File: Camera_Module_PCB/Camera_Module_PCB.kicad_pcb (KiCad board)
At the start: 4 copper layers, 118 parts, among them J1 SS-52400-002, J2 Conn_01x02, J3 FFC2A32-24-T, SW1 SW_DIP_x01, SW2 SW_Push, SW3 SW_Push, U2 ESP32-S3R8, U4 MAX98357AETE_T, U5 AP3032KTR-G1, Y1 Q40,0-JXS10-8-10/10-FU-LF1

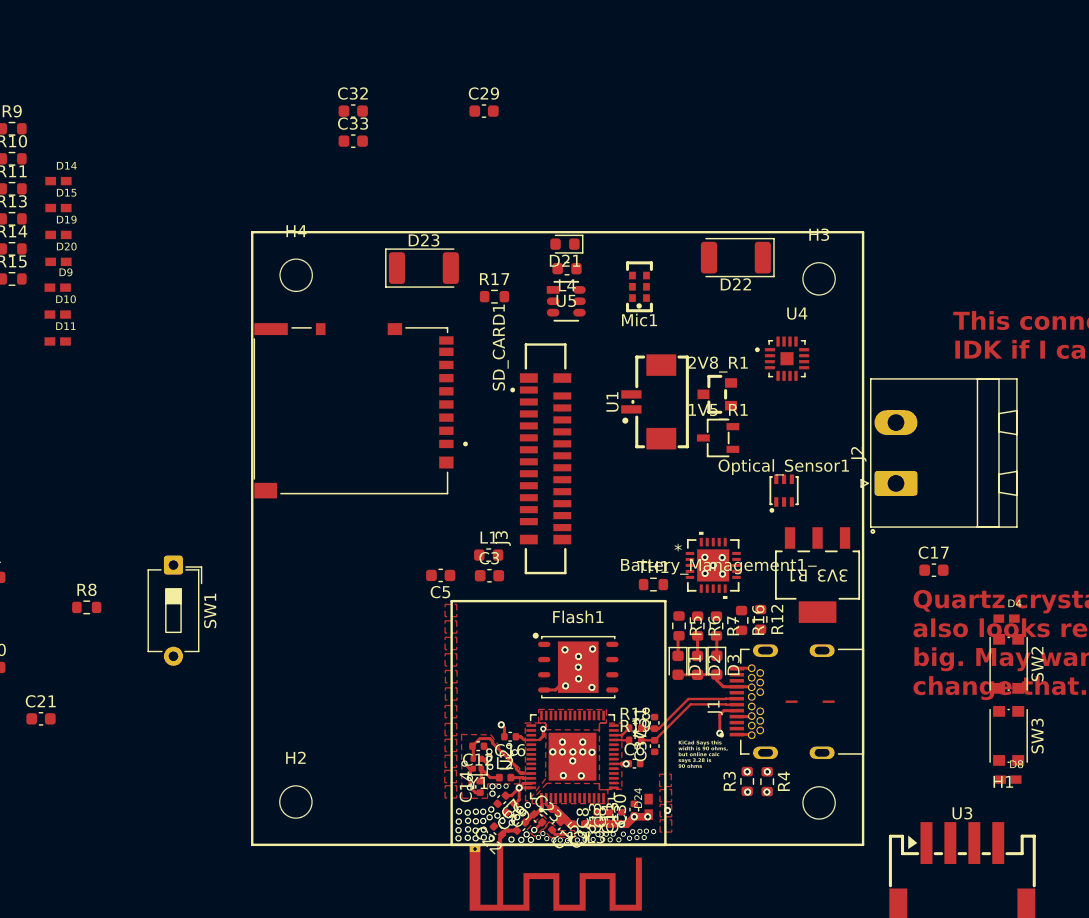
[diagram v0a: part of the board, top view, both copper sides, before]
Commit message: Finished Power Supply
The power supply was finished for the ESP32 Chip and the board as a whole. A large plain was constructed in the third layer of the PCB to hold the 3.3V power supply from the regulator. Multiple traces have begun to be routed out of the ESP32 chip to be connected later on.
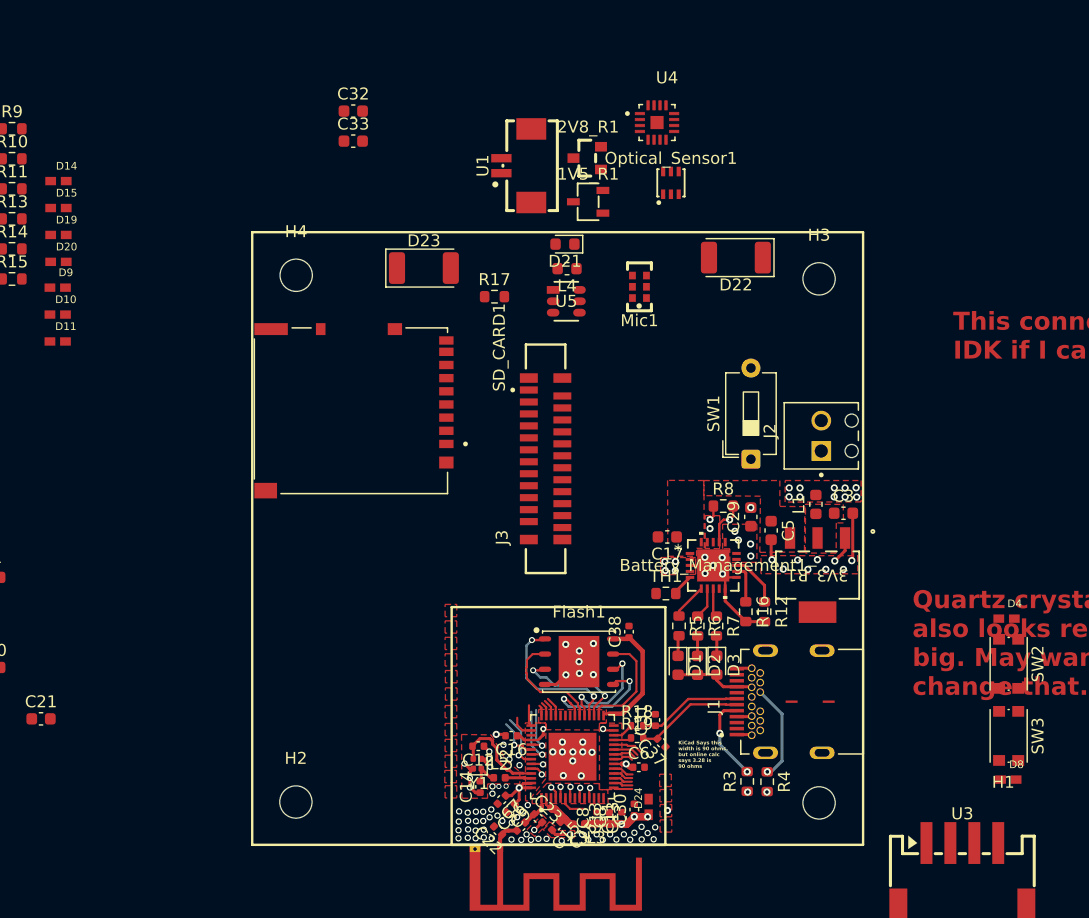
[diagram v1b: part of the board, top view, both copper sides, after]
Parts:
- added C38: 10uF, Capacitor_SMD:C_0402_1005Metric, F.Cu at (133.1, 84.2)
- J2: footprint Connector_Phoenix_MSTB:PhoenixContact_MSTBA_2,5_2-G-5,08_1x02_P5.08mm_Horizontal -> ESP32CAM_Foorprints:PHOENIX_1725656
- moved R8 53.9 mm to (141.0, 73.7)
- moved SW1 49.1 mm to (143.3, 69.8), turned to 90 degrees
- moved C29 40.6 mm to (143.3, 74.6), turned to 90 degrees
- moved C3 30.0 mm to (151.0, 74.3)
- moved C5 27.9 mm to (145.0, 75.7), turned to -90 degrees
- moved L1 27.7 mm to (148.7, 73.6), turned to 90 degrees
- moved Optical_Sensor1 27.4 mm to (136.6, 46.7)
- moved U4 22.5 mm to (135.4, 41.6)
- moved 2V8_R1 22.5 mm to (129.6, 44.6)
- moved U1 22.5 mm to (123.7, 45.2)
- moved 1V5_R1 22.5 mm to (129.7, 48.3)
- moved C17 22.5 mm to (136.3, 76.3), turned to 180 degrees
- moved J2 3.37 mm to (152.3, 70.6)
- moved TH1 1.28 mm to (136.2, 81.0)
- moved R16 0.81 mm to (142.8, 82.5)
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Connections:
- U2 pad 13: /SDA -> unconnected-(U2-GPIO8-Pad13)
- U2 pad 14: /SCL -> unconnected-(U2-GPIO9-Pad14)
- U2 pad 36: /Light_INT -> unconnected-(U2-SPICLK_N-Pad36)
- U2 pad 37: /LED_CT -> unconnected-(U2-SPICLK_P-Pad37)
- U2 pad 39: unconnected-(U2-GPIO34-Pad39) -> /Light_INT
- U2 pad 40: unconnected-(U2-GPIO35-Pad40) -> /LED_CT
- U2 pad 41: unconnected-(U2-GPIO36-Pad41) -> /SDA
- U2 pad 42: unconnected-(U2-GPIO37-Pad42) -> /SCL
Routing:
- net GND: track 16.4 -> 34.3 mm, vias 93 -> 96
- net Net-(Flash1-CS): track 0.00 -> 12.6 mm, vias 0 -> 2
- net /VDD_SPI: track 0.00 -> 10.6 mm
- net Net-(Flash1-DI(IO0)): track 0.00 -> 10.5 mm, vias 0 -> 2
- net /SPIWP: track 0.00 -> 9.92 mm, vias 0 -> 2
- net /Power Supply/CHG_EN: track 0.00 -> 9.61 mm, vias 0 -> 1
- net Net-(Flash1-DO(IO1)): track 0.00 -> 9.52 mm
- net /SPIHD: track 0.00 -> 9.05 mm
- net /SPICLK: track 0.00 -> 8.90 mm, vias 0 -> 2
- net /Power Supply/5V_USB: track 8.16 -> 15.7 mm, vias 0 -> 6
- net /LRCLK: track 0.00 -> 7.11 mm, vias 0 -> 1
- net /BCLK: track 0.00 -> 6.51 mm, vias 0 -> 1
- net Net-(U2-U0TXD): track 0.00 -> 4.96 mm, vias 0 -> 1
- net Net-(U2-U0RXD): track 0.00 -> 4.66 mm, vias 0 -> 1
- net Net-(Battery_Management1-PROG1): track 0.00 -> 4.42 mm
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- added copper zone on F.Cu, net /Power Supply/5V_USB
- added copper zone on In2.Cu, net /Power Supply/5V_USB
- added copper zone on F.Cu, net /Power Supply/VBAT
- added copper zone on In2.Cu, net /Power Supply/VBAT
- added copper zone on F.Cu, net Net-(3V3_R1-OUTPUT)
- added copper zone on F.Cu, net V_OUT_BM

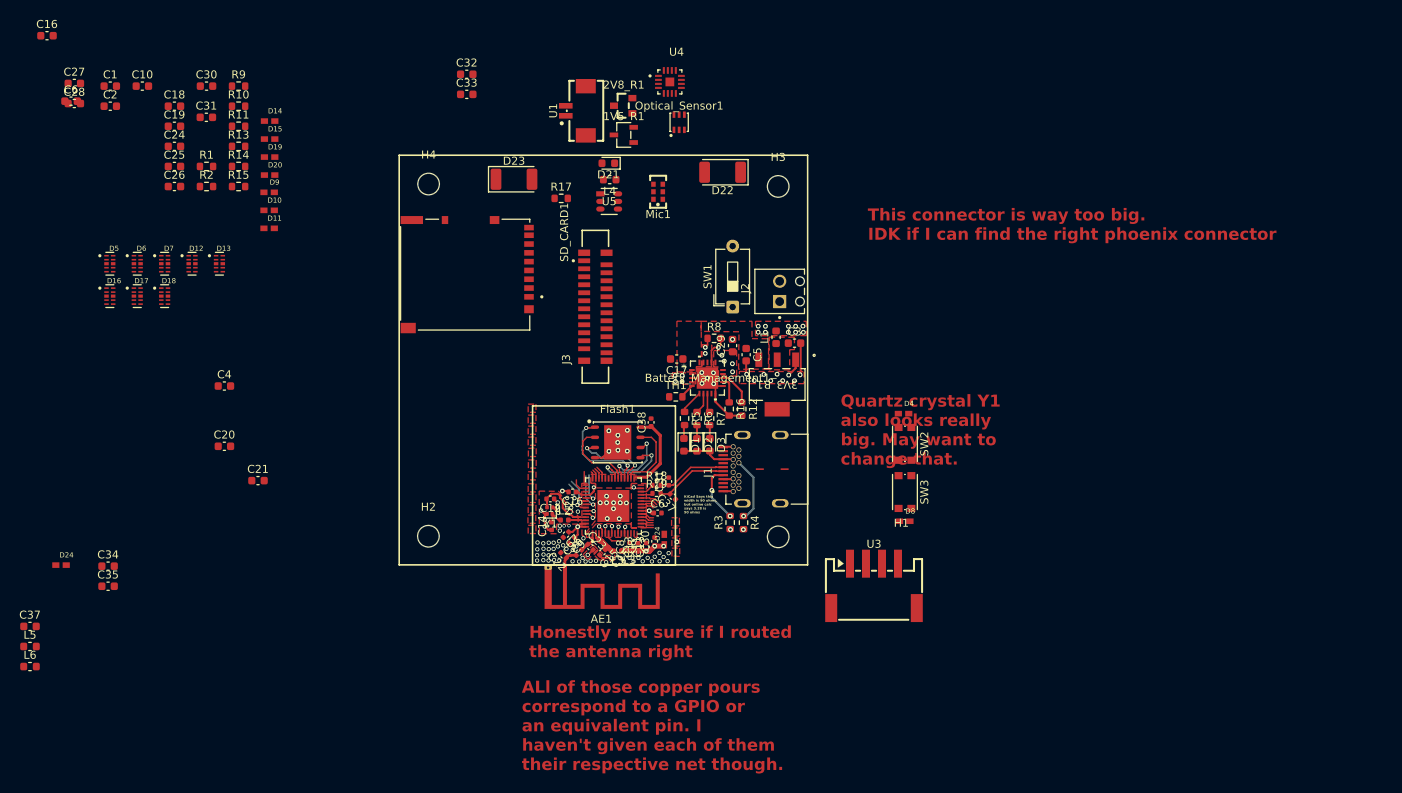
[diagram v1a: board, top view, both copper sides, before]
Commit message: Continued General Component Layout
More components were placed in general areas where they are predicted to remain. The two LDO voltage regulators for the camera power supply were connected to the main output voltage of the battery manager. The camera FFC connection along with other components were moved around the prepare for connections.
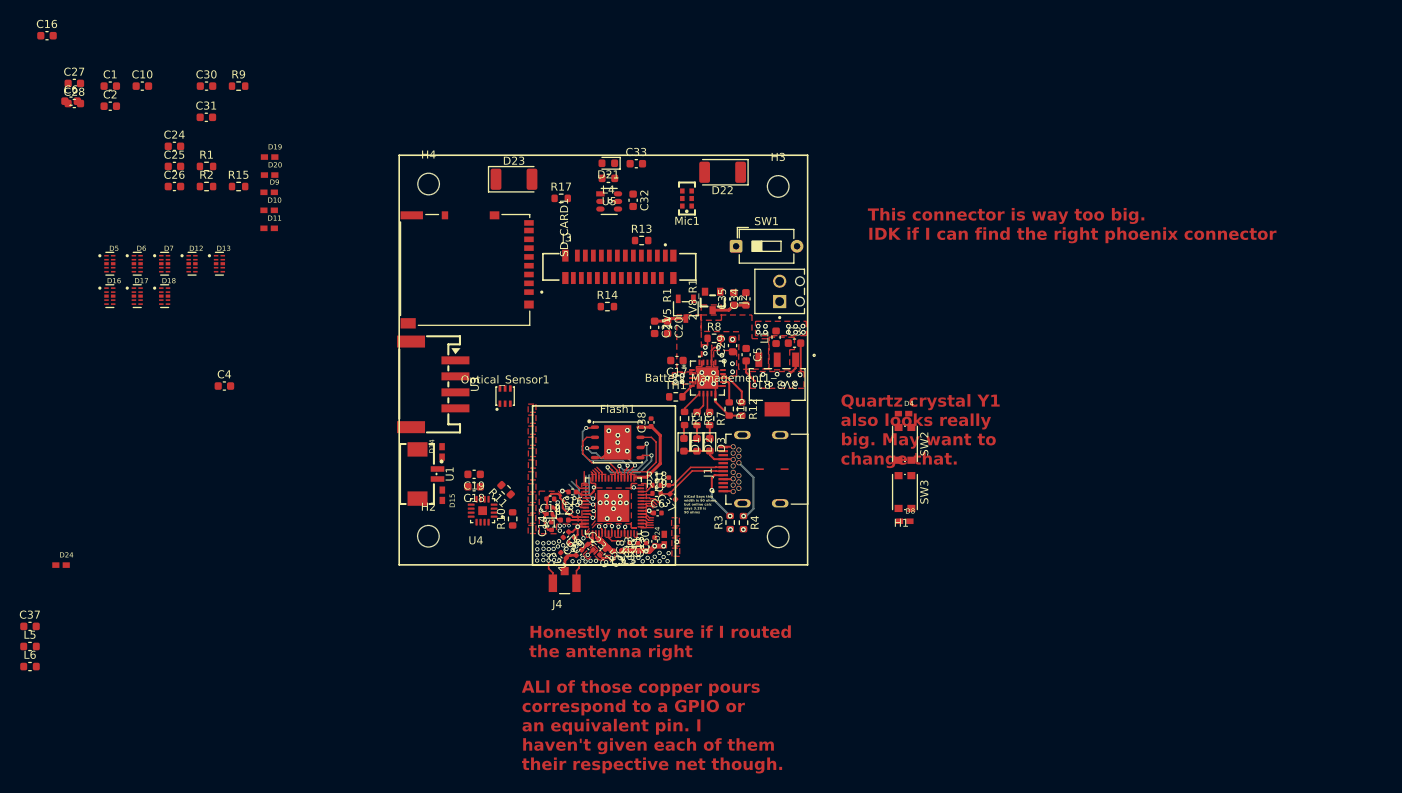
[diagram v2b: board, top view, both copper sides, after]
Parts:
- removed AE1: Antenna, RF_Antenna:Texas_SWRA117D_2.4GHz_Left
- added J4: U.FL-R-SMT-1_80_, ESP32CAM_Foorprints:HIROSE_U.FL-R-SMT-1_80_, F.Cu at (122.3, 104.3)
- moved C34 86.4 mm to (144.9, 68.8), turned to 90 degrees
- moved C35 86.1 mm to (143.4, 68.8), turned to 90 degrees
- moved R10 61.9 mm to (115.8, 96.3), turned to 90 degrees
- moved U3 60.6 mm to (105.9, 79.4), turned to -90 degrees
- moved C18 60.5 mm to (111.0, 92.2), turned to 180 degrees
- moved U4 58.5 mm to (112.0, 95.2), turned to 180 degrees
- moved C19 57.4 mm to (111.0, 90.7), turned to 180 degrees
- moved C20 57.3 mm to (135.1, 72.3), turned to -90 degrees
- moved R11 56.4 mm to (115.0, 92.6), turned to 135 degrees
- moved C21 53.2 mm to (133.5, 72.3), turned to -90 degrees
- moved R13 51.7 mm to (131.9, 61.5)
- moved D15 49.5 mm to (107.0, 93.3), turned to -90 degrees
- moved R14 49.3 mm to (127.6, 69.7)
- moved U1 49.0 mm to (105.1, 90.6), turned to -90 degrees
- moved D14 46.6 mm to (107.0, 87.9), turned to 90 degrees
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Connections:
- 1V5_R1 pad 3: +3.3V -> V_OUT_BM
- 2V8_R1 pad 3: +3.3V -> V_OUT_BM
- C20 pad 1: +3.3V -> V_OUT_BM
- C21 pad 1: +3.3V -> V_OUT_BM
- C22 pad 1: Net-(AE1-A) -> Net-(C22-Pad1)
- C34 pad 1: +3.3V -> V_OUT_BM
- C35 pad 1: +3.3V -> V_OUT_BM
- C36 pad 1: Net-(AE1-A) -> Net-(C22-Pad1)
- D15 pad 1: GND -> Net-(U4-OUTP)
- D15 pad 2: Net-(U4-OUTP) -> GND
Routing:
- net V_OUT_BM: track 0.00 -> 8.45 mm
- net /Power Supply/CHG_EN: track 9.61 -> 17.4 mm
- net GND: track 34.3 -> 42.0 mm, vias 96 -> 95
- net Net-(C22-Pad1): track 0.00 -> 1.55 mm
- net Net-(AE1-A): track 1.55 -> 0.00 mm
- net /OV: track 0.00 -> 0.98 mm, vias 0 -> 1

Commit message: Finished General Layout
All components have their general location on the PCB with some wiggle room for most parts to move around. Traces are what is left to complete the board.
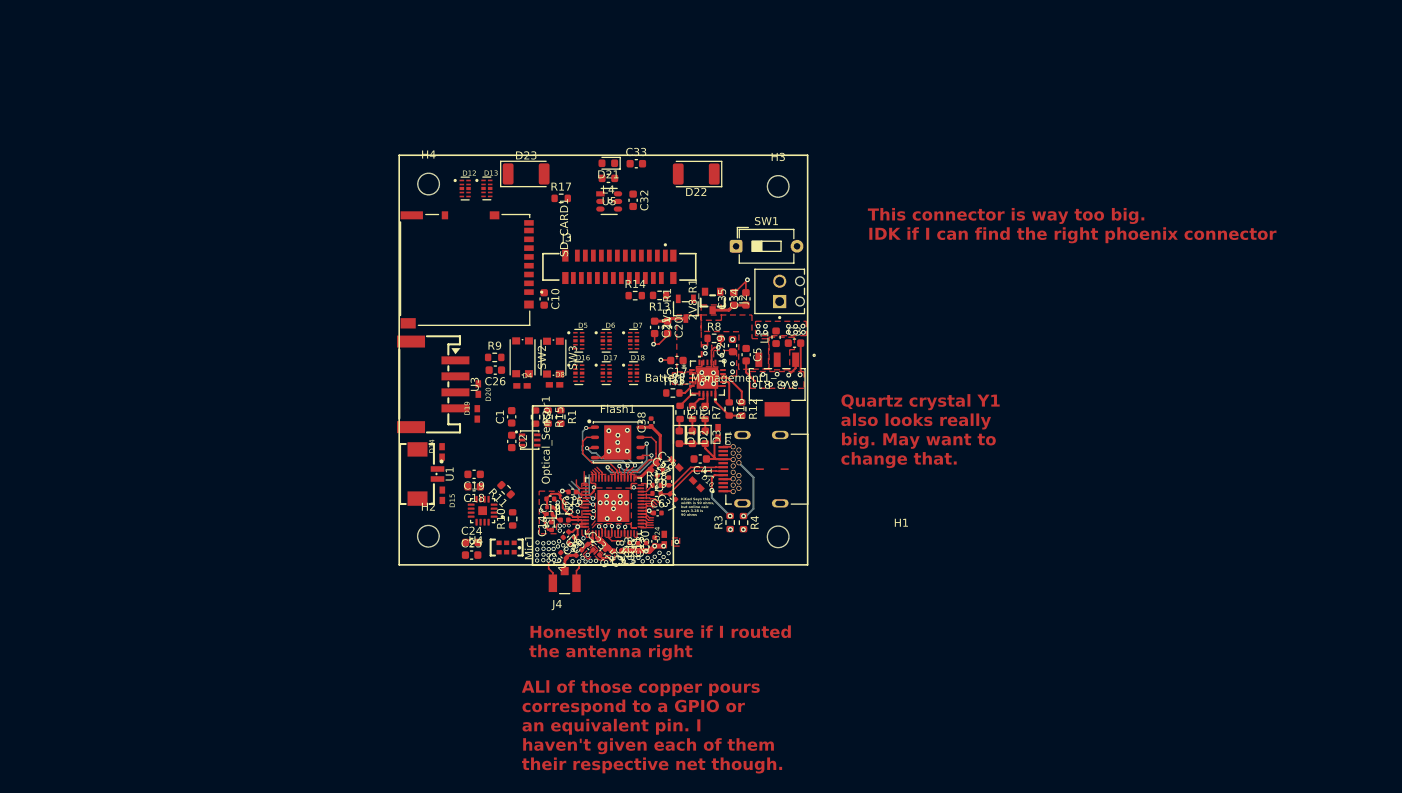
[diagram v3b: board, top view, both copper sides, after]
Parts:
- removed the C16 at (57.6, 35.9)
- removed the C30 at (77.5, 42.2)
- removed the C31 at (77.5, 46.1)
- removed the C37 at (55.5, 109.7)
- removed the C6 at (60.6, 44.0)
- removed the D24 at (59.3, 102.0)
- removed L5, L6: L, Inductor_SMD:L_0603_1608Metric
- C27, C28: footprint Capacitor_SMD:C_0603_1608Metric -> Capacitor_SMD:C_0402_1005Metric
- moved C27 87.4 mm to (133.5, 90.5), turned to -45 degrees
- moved C28 86.2 mm to (134.2, 89.8), turned to -45 degrees
- moved C2 65.4 mm to (115.7, 86.6), turned to -90 degrees
- moved C1 65.0 mm to (115.7, 83.5), turned to 90 degrees
- moved D10 63.5 mm to (138.8, 91.9), turned to -45 degrees
- moved C24 61.9 mm to (110.7, 99.2)
- moved D11 61.7 mm to (141.5, 85.5), turned to -90 degrees
- moved C25 61.2 mm to (110.7, 100.8)
- moved D9 61.1 mm to (136.2, 89.4), turned to 135 degrees
- moved C4 60.2 mm to (139.2, 88.8), turned to 180 degrees
- moved D18 59.4 mm to (130.9, 78.0)
- moved D7 59.4 mm to (130.9, 74.0)
- moved D16 59.4 mm to (124.0, 78.0)
- moved D17 59.4 mm to (127.5, 78.0)
- moved D5 59.4 mm to (124.0, 74.0)
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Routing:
- net GND: track 42.0 -> 50.9 mm, vias 95 -> 98
- net /Power Supply/5V_USB: track 15.7 -> 21.5 mm
- removed copper zone on F.Cu, net /RST
